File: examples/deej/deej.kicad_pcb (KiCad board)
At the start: 4 copper layers, 293.4 x 207 mm, 27 parts, among them U1 2821, U2 5836

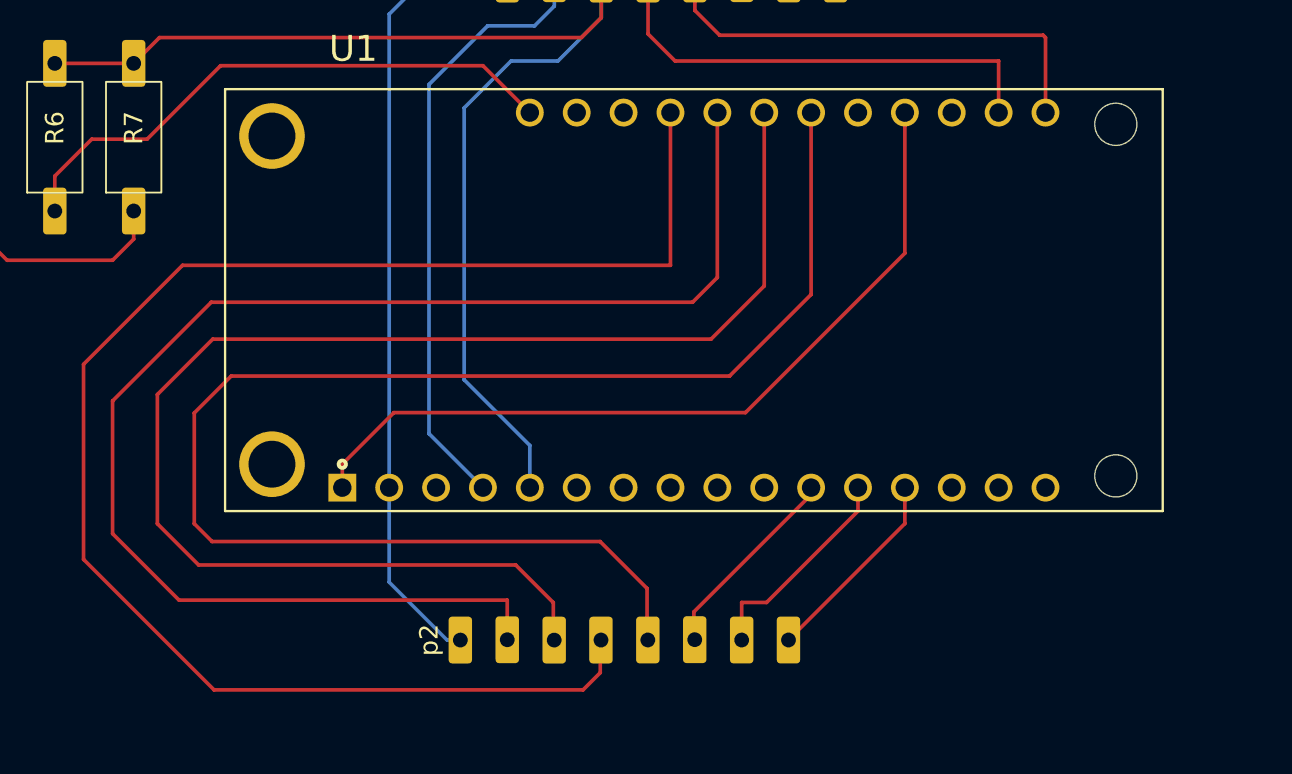
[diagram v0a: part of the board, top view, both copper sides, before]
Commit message: updated deej example with traces for input power
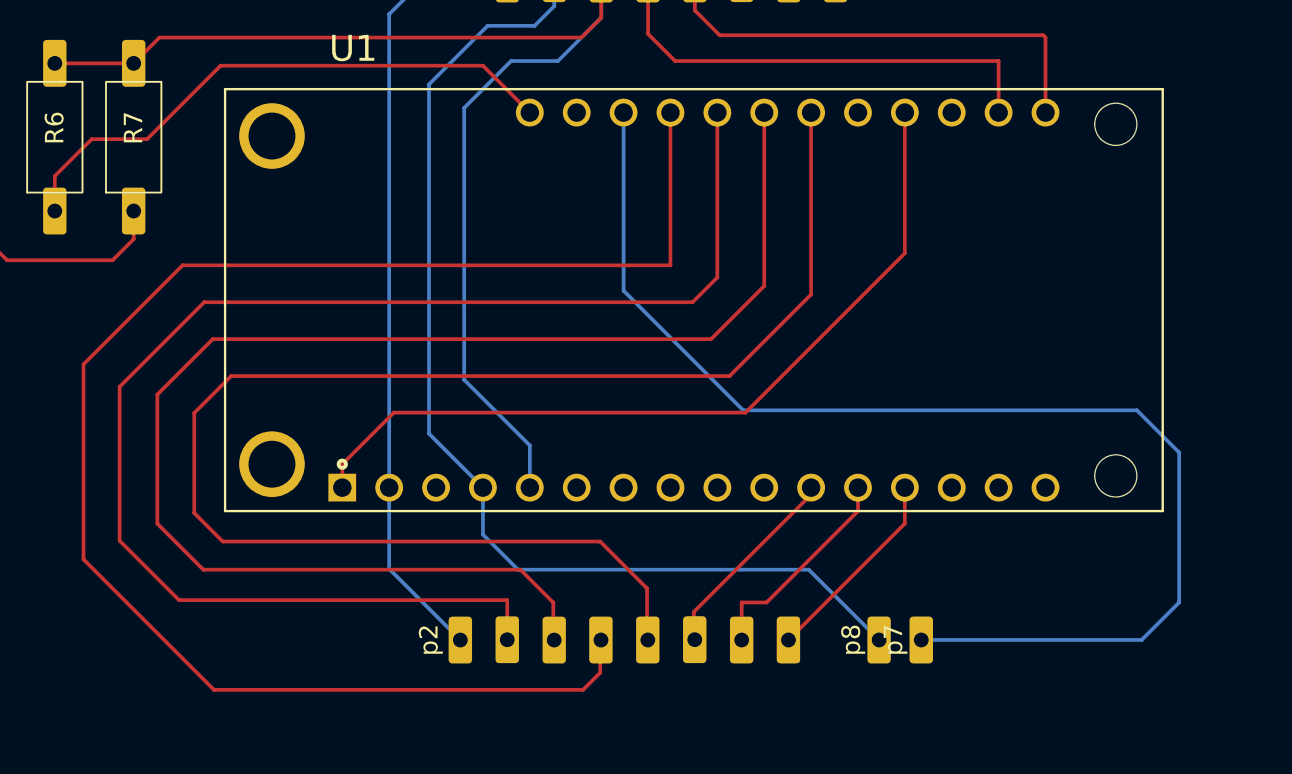
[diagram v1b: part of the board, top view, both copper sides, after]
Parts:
- added p7: CHRG, Adafruit:Through Hole 0.1in 1 Pin, F.Cu at (78.7, 190.5)
- added p8: GND, Adafruit:Through Hole 0.1in 1 Pin, F.Cu at (76.5, 190.5)
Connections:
- U1 pad 19: unconnected-(U1-VUSB-Pad19) -> /CHRG
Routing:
- net /CHRG: track 0.00 -> 66.3 mm
- net /GND: track 410.1 -> 436.4 mm

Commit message: fix deej pcb design
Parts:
- p8: value GND -> CHRG
- moved p4 4.25 mm to (53.8, 104.3)
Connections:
- p3 pad 3: Net-(U1-ADC) -> /SCL
- p3 pad 4: /SCL -> /SDA
- p3 pad 5: /SDA -> unconnected-(p3-p-Pad5)
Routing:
- net Net-(U1-ADC): track 66.3 -> 47.7 mm, vias 0 -> 1
- net /SDA: track 157.6 -> 150.3 mm
- net /GND: track 436.4 -> 437.6 mm

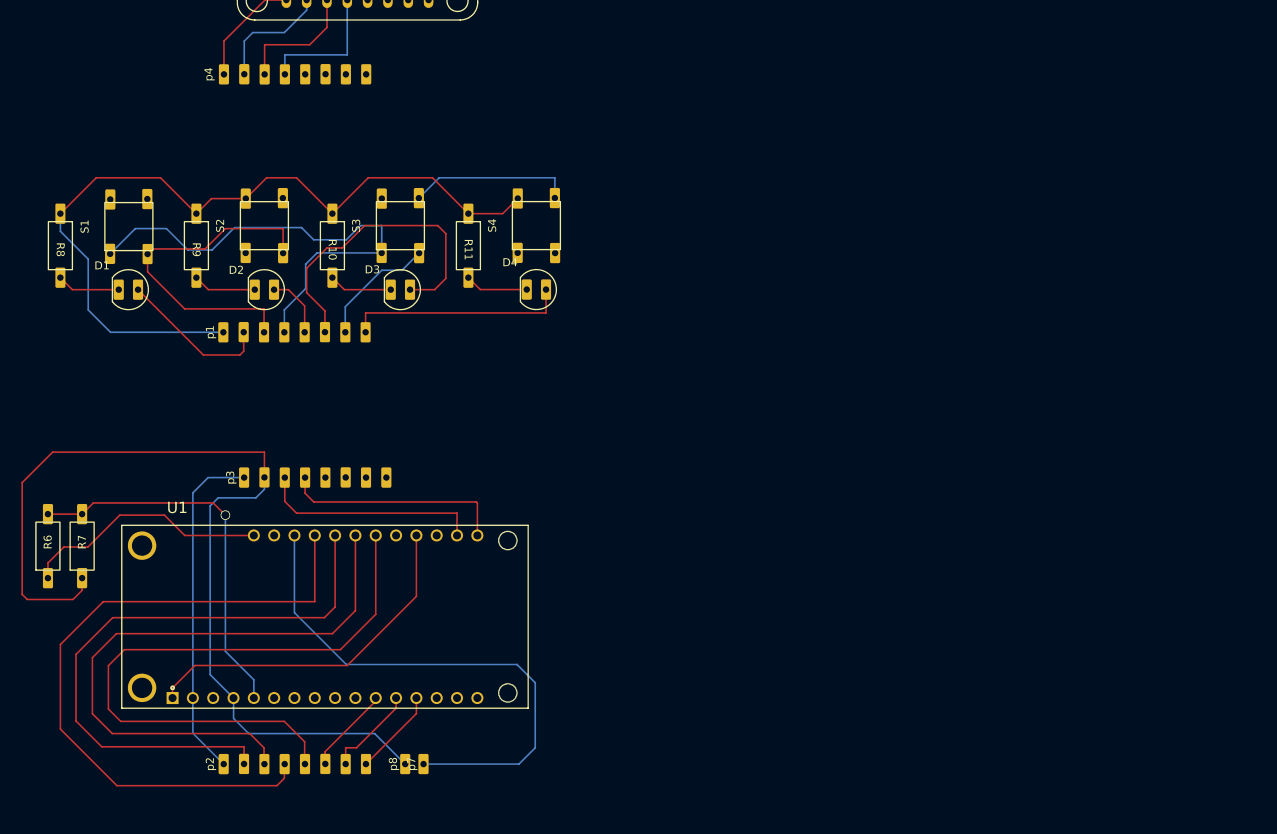
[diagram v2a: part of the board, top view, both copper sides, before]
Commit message: add MCP23008 GPIO over I2C chip
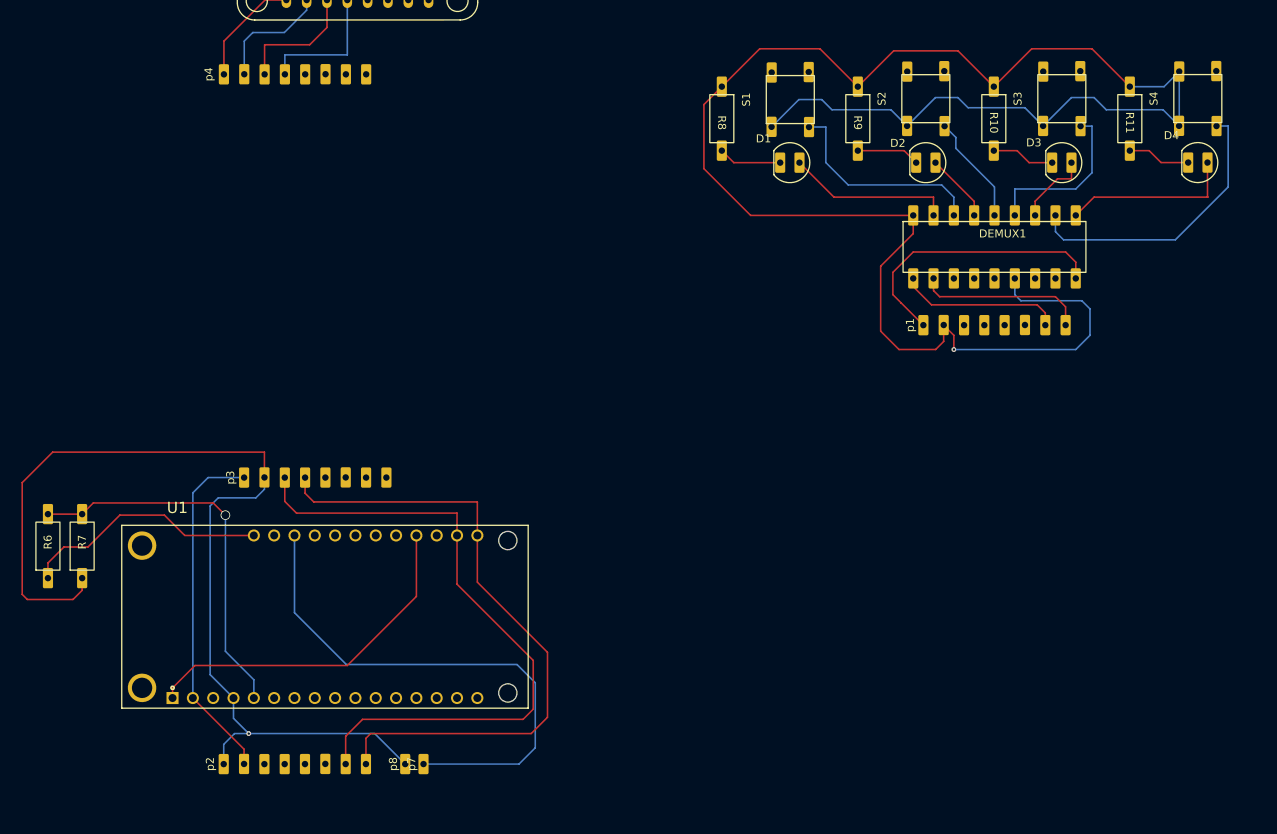
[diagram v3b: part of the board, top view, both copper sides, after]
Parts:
- added DEMUX1: DEMUX1, Adafruit:DEMUX_MCP23008_593, F.Cu at (150.1, 125.9)
- moved p1 87.5 mm to (141.2, 135.6)
- moved D1 84.2 mm to (124.5, 115.3)
- moved D2 84.2 mm to (141.5, 115.3)
- moved D3 84.2 mm to (158.5, 115.3)
- moved D4 84.2 mm to (175.5, 115.3)
- moved R10 84.2 mm to (150.0, 109.8)
- moved R11 84.2 mm to (167.0, 109.8)
- moved R8 84.2 mm to (116.0, 109.8)
- moved R9 84.2 mm to (133.0, 109.8)
- moved S1 84.2 mm to (124.6, 107.4)
- moved S2 84.2 mm to (141.5, 107.3)
- moved S3 84.2 mm to (158.5, 107.3)
- moved S4 84.2 mm to (175.5, 107.3)
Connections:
- D1 pad 2: /D1 -> Net-(D1-N)
- D2 pad 2: /D2 -> Net-(D2-N)
- D3 pad 2: /D3 -> Net-(D3-N)
- D4 pad 2: /D4 -> Net-(D4-N)
- S1 pad 1: /TMP -> /3v
- S1 pad 2: /S12 -> Net-(DEMUX1-GP6)
- S2 pad 2: /S12 -> Net-(DEMUX1-GP4)
- S3 pad 1: /TMP -> /3v
- S3 pad 2: /S34 -> Net-(DEMUX1-GP3)
- S4 pad 2: /S34 -> Net-(DEMUX1-GP1)
- U1 pad 11: /D3 -> unconnected-(U1-SCK-Pad11)
- U1 pad 12: /S34 -> unconnected-(U1-MOSI-Pad12)
- U1 pad 13: /D4 -> unconnected-(U1-MIS0-Pad13)
- U1 pad 20: /TMP -> unconnected-(U1-GPIO14-Pad20)
- U1 pad 21: /D1 -> unconnected-(U1-GPIO12-Pad21)
- U1 pad 22: /S12 -> unconnected-(U1-GPIO13-Pad22)
- U1 pad 23: /D2 -> unconnected-(U1-GPIO15-Pad23)
- p1 pad 1: /3v -> /GND
- p1 pad 2: /D1 -> /3v
- p1 pad 3: /S12 -> unconnected-(p1-p-Pad3)
- p1 pad 4: /TMP -> unconnected-(p1-p-Pad4)
- p1 pad 5: /D2 -> unconnected-(p1-p-Pad5)
- p1 pad 6: /D3 -> unconnected-(p1-p-Pad6)
- p1 pad 7: /S34 -> /SCL
- p1 pad 8: /D4 -> /SDA
- p2 pad 1: /3v -> /GND
- p2 pad 2: /D1 -> /3v
- p2 pad 3: /S12 -> unconnected-(p2-p-Pad3)
- p2 pad 4: /TMP -> unconnected-(p2-p-Pad4)
- p2 pad 5: /D2 -> unconnected-(p2-p-Pad5)
- p2 pad 6: /D3 -> unconnected-(p2-p-Pad6)
- p2 pad 7: /S34 -> /SCL
- p2 pad 8: /D4 -> /SDA
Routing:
- net /3v: track 523.7 -> 750.6 mm, vias 0 -> 1
- net /TMP: track 188.5 -> 0.00 mm
- net /S12: track 163.8 -> 0.00 mm
- net /SCL: track 147.3 -> 310.8 mm
- net /SDA: track 150.3 -> 313.0 mm
- net /GND: track 437.6 -> 572.3 mm, vias 0 -> 1
- net /S34: track 134.0 -> 0.00 mm
- net /D1: track 125.9 -> 0.00 mm
- net /D3: track 124.3 -> 0.00 mm
- net /D2: track 117.4 -> 0.00 mm
- net /D4: track 110.9 -> 0.00 mm
- net Net-(DEMUX1-GP1): track 0.00 -> 42.7 mm
- net Net-(DEMUX1-GP6): track 0.00 -> 33.5 mm
- net Net-(DEMUX1-GP3): track 0.00 -> 27.9 mm
- net Net-(D4-N): track 0.00 -> 21.8 mm
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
